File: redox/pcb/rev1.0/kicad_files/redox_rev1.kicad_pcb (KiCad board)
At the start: 2 copper layers, 162.2 x 126.5 mm, 86 parts, among them K0 KEYSW, K1 KEYSW, K10 KEYSW, K11 KEYSW, K12 KEYSW, K13 KEYSW, K14 KEYSW, K15 KEYSW, K16 KEYSW, K2 KEYSW, K20 KEYSW, K21 KEYSW, K22 KEYSW, K23 KEYSW, K24 KEYSW, K25 KEYSW, K26 KEYSW, K3 KEYSW, K30 KEYSW, K31 KEYSW, K32 KEYSW, K33 KEYSW, K34 KEYSW, K35 KEYSW, K36 KEYSW, K4 KEYSW, K40 KEYSW, K41 KEYSW, K42 KEYSW, K43 KEYSW, K44 KEYSW, K45 KEYSW, K46 KEYSW, K5 KEYSW, K6 KEYSW, U1 ProMicro

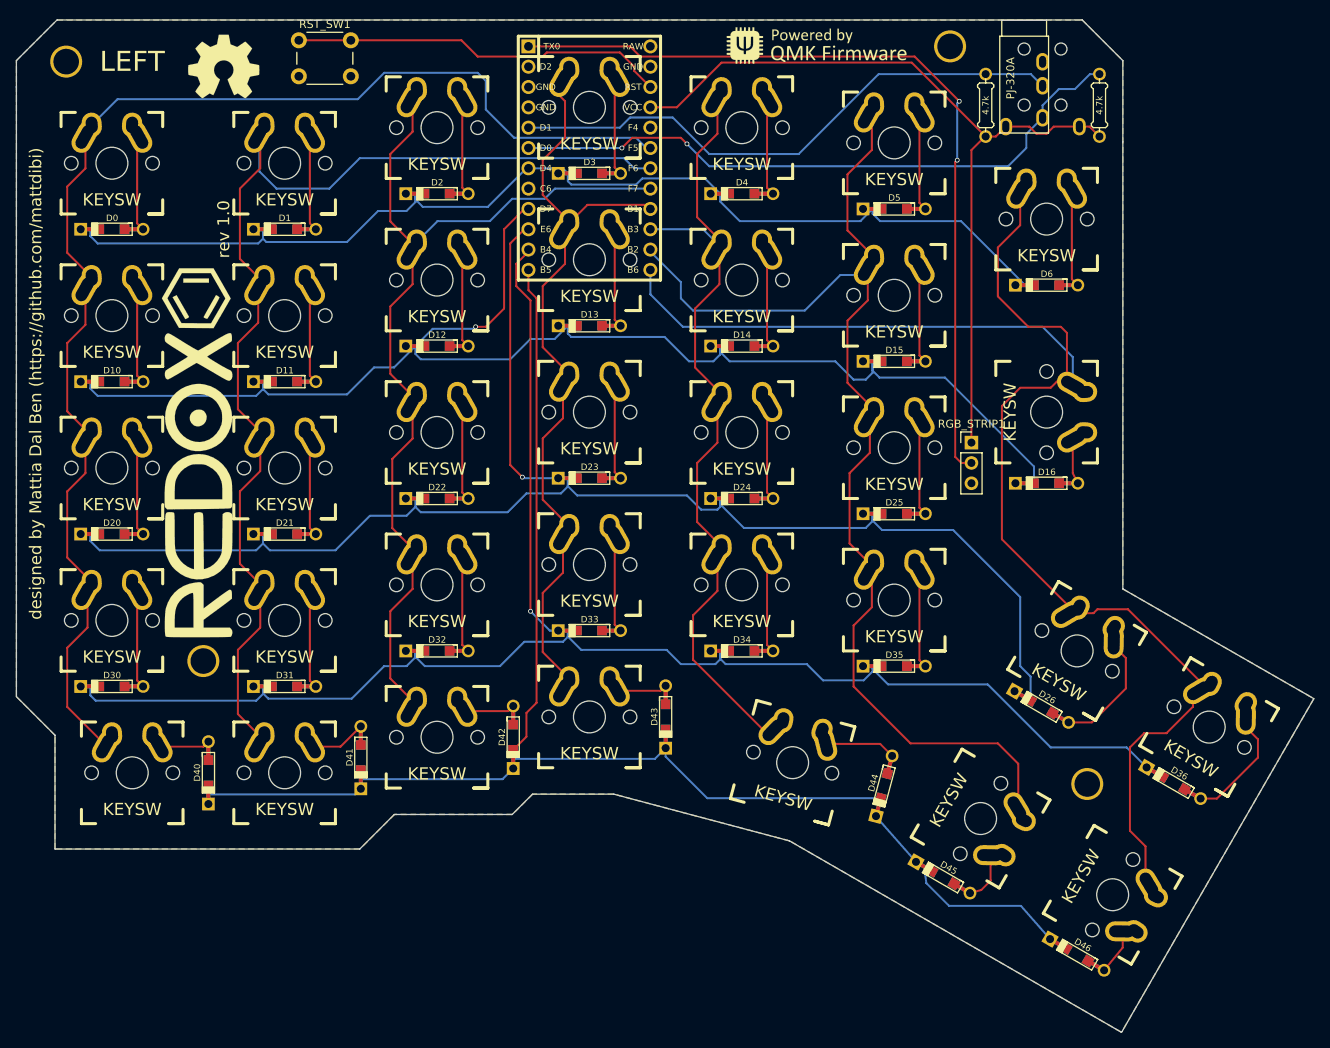
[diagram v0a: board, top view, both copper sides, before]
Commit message: hotswap pcb not verified yet
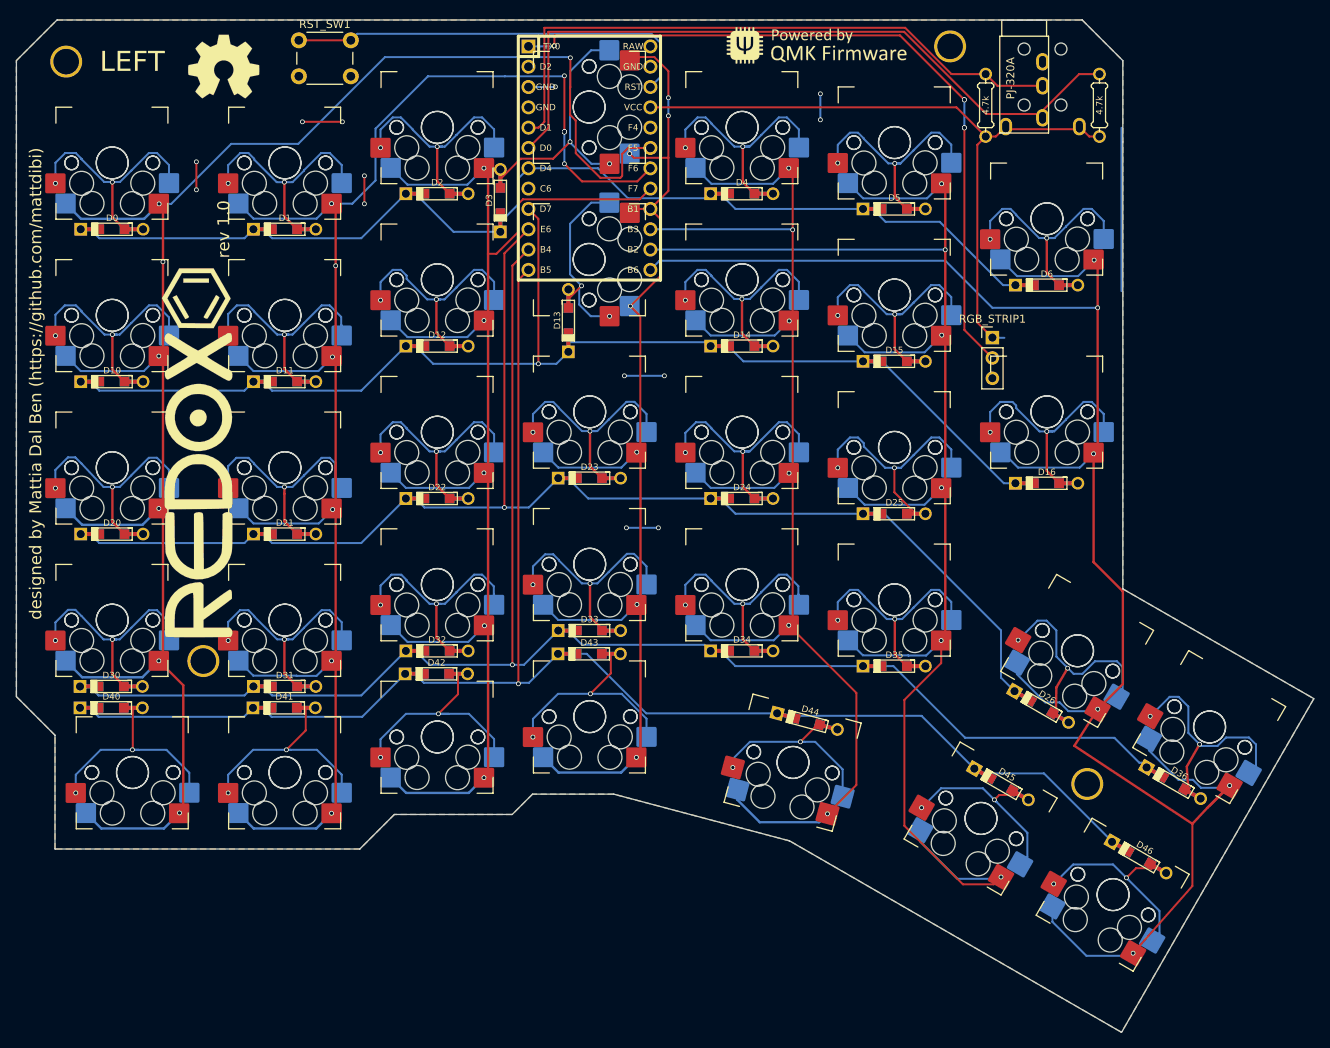
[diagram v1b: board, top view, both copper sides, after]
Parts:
- D0, D1, D10, D11, D12, D13, D14, D15, D16, D2, D20, D21, D22, D23, D24, D25, D26, D3, D30, D31, D32, D33, D34, D35, D36, D4, D40, D41, D42, D43, D44, D45, D46, D5, D6: footprint Keebio-Parts:Diode-dual -> redox_footprints:Diode-dual
- K0, K10, K20, K30, K44: footprint myparts:Mx_Alps_125-dualside -> redox_footprints:my_Mx_Alps_100-dualside-Hotswap
- K1, K11, K12, K13, K14, K15, K2, K21, K22, K23, K24, K25, K26, K3, K31, K32, K33, K34, K35, K36, K4, K40, K41, K42, K43, K5, K6: footprint canadian_footprints:Mx_Alps_100-dualside -> redox_footprints:my_Mx_Alps_100-dualside-Hotswap
- K16, K45, K46: footprint canadian_footprints:Mx_Alps_150-dualsided -> redox_footprints:my_Mx_Alps_100-dualside-Hotswap
- R1, R2: footprint Keebio-Parts:Resistor-Compact -> redox_footprints:Resistor-Compact
- RGB_STRIP1: footprint Pin_Headers:Pin_Header_Straight_1x03_Pitch2.54mm -> redox_footprints:Pin_Header_Straight_1x03_Pitch2.54mm
- RST_SW1: footprint Buttons_Switches_ThroughHole:SW_PUSH_6mm_h4.3mm -> redox_footprints:SW_PUSH_6mm_h4.3mm
- TRRS1: footprint Keebio-Parts:TRRS-PJ-320A-dual -> redox_footprints:TRRS-PJ-320A-dual
- U1: footprint Keebio-Parts:ArduinoProMicro -> redox_footprints:ArduinoProMicro
- moved D40 14.6 mm to (91.3, 134.8), turned to 180 degrees
- moved D46 14.4 mm to (219.8, 153.4)
- moved D45 13.8 mm to (202.6, 144.3)
- moved RGB_STRIP1 13.4 mm to (201.5, 88.5)
- moved D44 12.5 mm to (178.4, 136.4), turned to 165 degrees
- moved D42 12.5 mm to (132.0, 130.5), turned to 180 degrees
- moved D43 12.4 mm to (151.1, 128.0), turned to 180 degrees
- moved D3 11.6 mm to (140.0, 71.3), turned to -90 degrees
- moved D41 11.4 mm to (113.0, 134.8), turned to 180 degrees
- moved D13 2.71 mm to (148.5, 86.3), turned to -90 degrees
- moved D30 0.09 mm to (91.3, 132.1)
- turned K0 to 180 degrees
- turned K1 to 180 degrees
- turned K10 to 180 degrees
- turned K11 to 180 degrees
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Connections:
- U1 pad 2: Net-(U1-Pad2) -> unconnected-(U1-RX1/PD2-Pad2)
- U1 pad 20: Net-(U1-Pad20) -> unconnected-(U1-A3/PF4-Pad20)
- U1 pad 24: Net-(U1-Pad24) -> unconnected-(U1-RAW-Pad24)
- U1 pad 8: Net-(U1-Pad8) -> unconnected-(U1-5/PC6-Pad8)
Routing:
- net col4: track 103.1 -> 171.9 mm, vias 0 -> 6
- net col1: track 144.0 -> 207.0 mm, vias 0 -> 12
- net col0: track 167.6 -> 230.5 mm, vias 0 -> 7
- net col5: track 146.1 -> 202.8 mm, vias 0 -> 6
- net col6: track 184.3 -> 238.3 mm, vias 0 -> 6
- net col2: track 119.8 -> 170.3 mm, vias 0 -> 5
- net col3: track 97.8 -> 145.4 mm, vias 0 -> 7
- net GND: track 0.00 -> 27.8 mm, vias 0 -> 13
- net row1: track 169.3 -> 143.3 mm
- net Net-(D16-A): track 5.88 -> 31.2 mm, vias 0 -> 2
- net row2: track 188.9 -> 165.7 mm
- net Net-(D42-A): track 6.63 -> 28.6 mm, vias 0 -> 2
- net Net-(D43-A): track 6.63 -> 27.4 mm, vias 0 -> 2
- net Net-(D41-A): track 7.42 -> 28.1 mm, vias 0 -> 2
- net Net-(D40-A): track 6.63 -> 27.2 mm, vias 0 -> 2
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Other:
- net class Default removed
